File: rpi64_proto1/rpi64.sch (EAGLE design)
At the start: 115 parts, among them Q1 BSS123, Q2 BSS123

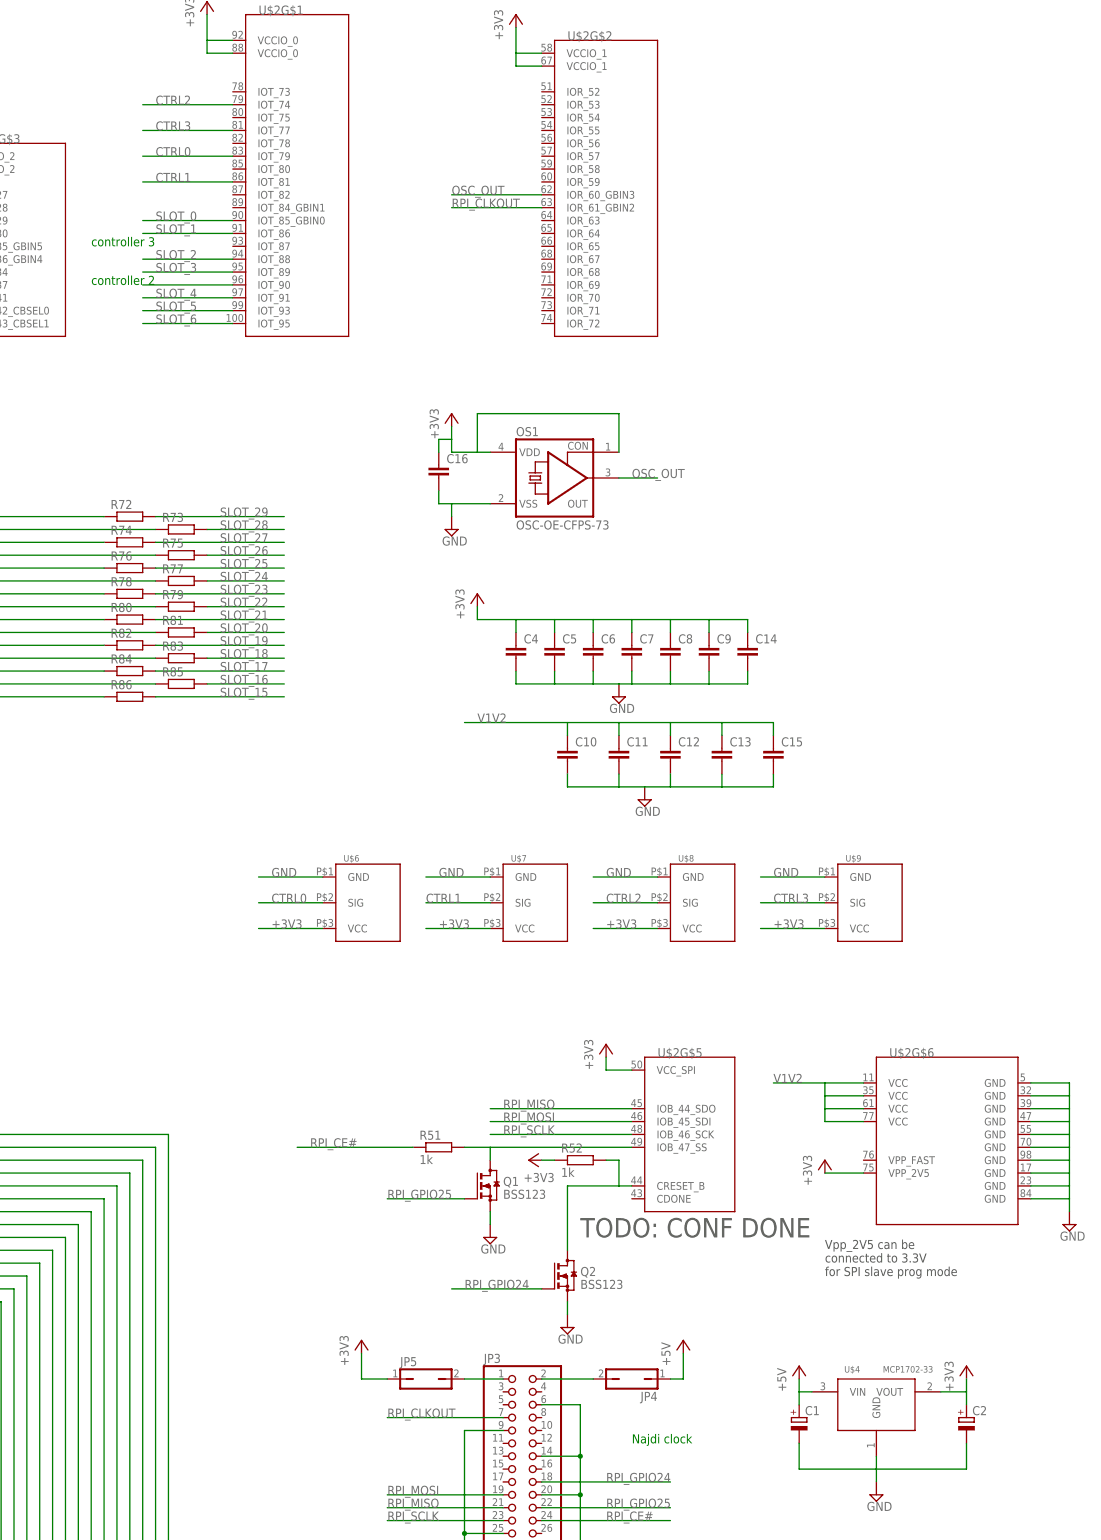
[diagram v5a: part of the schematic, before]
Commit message: Everything placed and routed
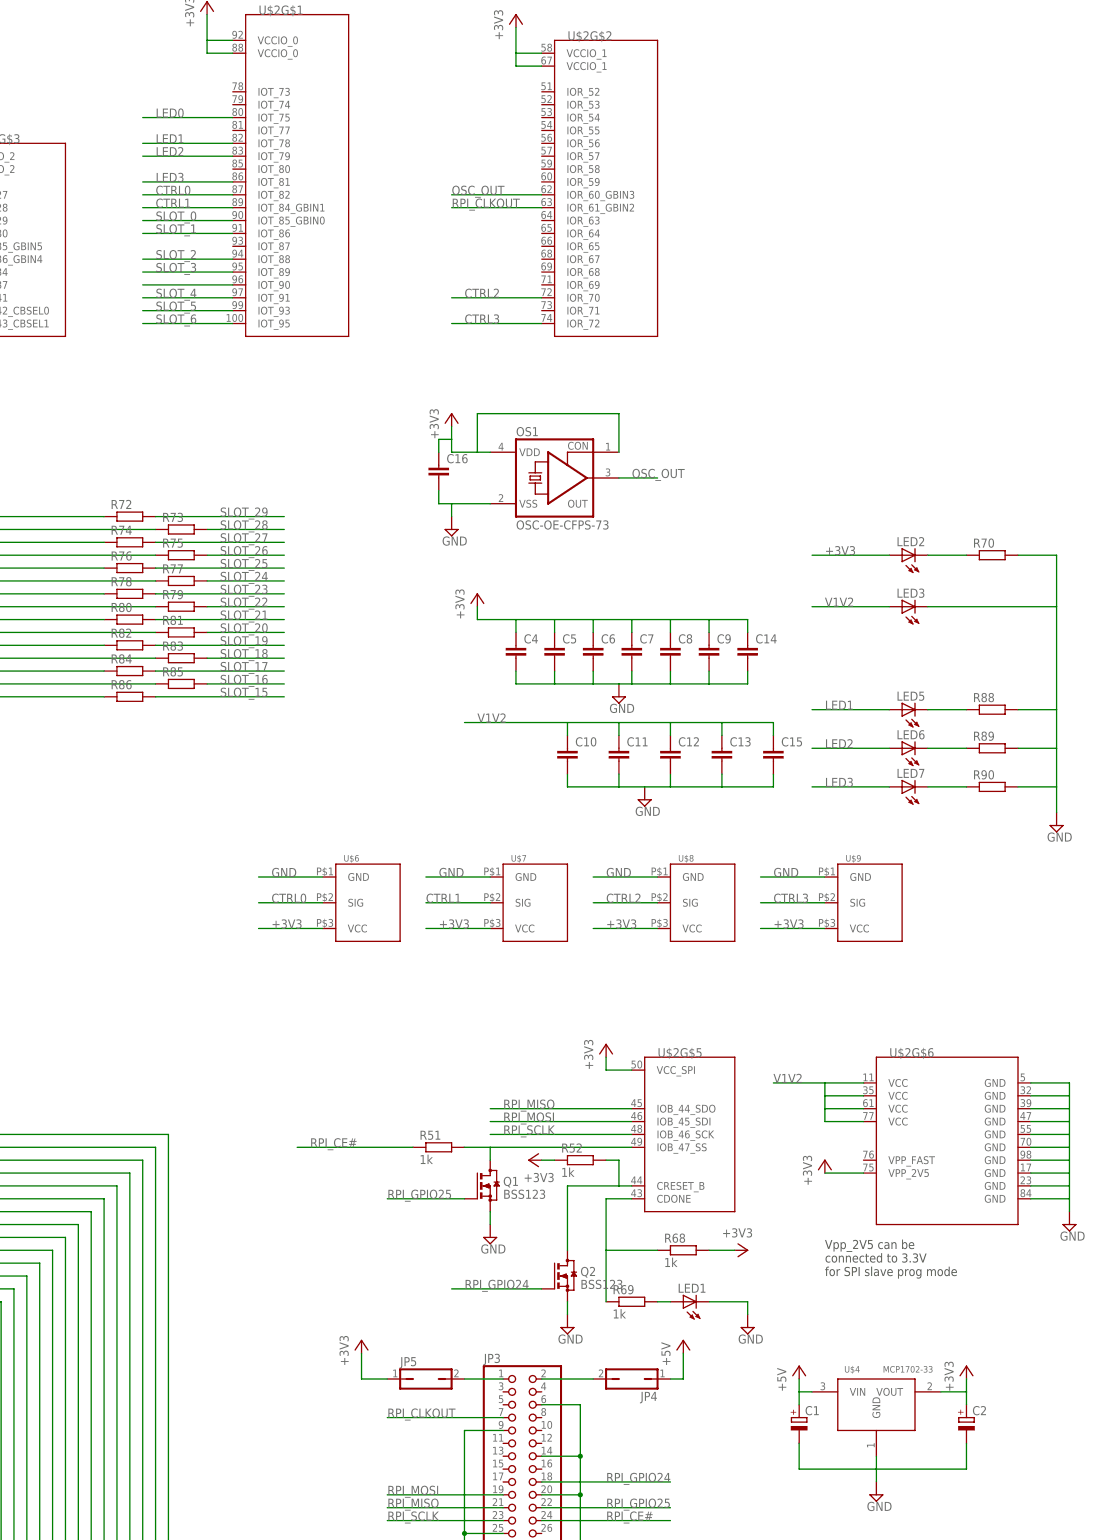
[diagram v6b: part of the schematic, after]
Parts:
- added LED1, LED2, LED3, LED5, LED6, LED7: (no value), led:LEDCHIPLED_0603
- added R68, R69: 1k, rcl:R-EU_R0603
- added R70, R88, R89, R90: (no value), rcl:R-EU_R0603
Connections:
- new net LED0: U$2G$1.IOT_75
- new net LED1: LED5.A, U$2G$1.IOT_78
- new net LED2: LED6.A, U$2G$1.IOT_79
- new net LED3: LED7.A, U$2G$1.IOT_81
- new net N$104: LED1.A, R69.2
- new net N$107: LED7.C, R90.1
- new net N$109: LED6.C, R89.1
- new net N$111: LED5.C, R88.1
- new net N$116: LED2.C, R70.1
- new net N$91: R68.1, R69.1, U$2G$5.CDONE
- net +3V3: now also LED2.A, R68.2
- net CTRL0: now also U$2G$1.IOT_82; no longer U$2G$1.IOT_79
- net CTRL1: now also U$2G$1.IOT_84_GBIN1; no longer U$2G$1.IOT_81
- net CTRL2: now also U$2G$2.IOR_70; no longer U$2G$1.IOT_74
- net CTRL3: now also U$2G$2.IOR_72; no longer U$2G$1.IOT_77
- net GND: now also LED1.C, LED3.C, R70.2, R88.2, R89.2, R90.2
- net V1V2: now also LED3.A
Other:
- note removed: "Najdi clock"
- note removed: "TODO: CONF DONE"
- note removed: "controller 2"
- note removed: "controller 3"

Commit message: Resolved DRC problems
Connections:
- removed net N$110: U$2G$1.IOT_90
- removed net N$113: U$2G$4.IOL_7A_GBIN6
- removed net N$114: U$2G$4.IOL_6B_GBIN7
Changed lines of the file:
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@@
 <pinref part="U$2" gate="G$6" pin="GND@9"/>
 <wire x1="388.62" y1="83.82" x2="396.24" y2="83.82" width="0.1524" layer="91"/>
+<junction x="396.24" y="104.14"/>
+<junction x="396.24" y="101.6"/>
+<junction x="396.24" y="99.06"/>
+<junction x="396.24" y="96.52"/>
+<junction x="396.24" y="93.98"/>
+<junction x="396.24" y="91.44"/>
+<junction x="396.24" y="88.9"/>
+<junction x="396.24" y="86.36"/>
+<junction x="396.24" y="83.82"/>
 </segment>
 <segment>
@@
 <wire x1="337.82" y1="167.64" x2="337.82" y2="165.1" width="0.1524" layer="91"/>
 <wire x1="337.82" y1="165.1" x2="327.66" y2="165.1" width="0.1524" layer="91"/>
+<junction x="307.34" y="165.1"/>
+<junction x="317.5" y="165.1"/>
+<junction x="327.66" y="165.1"/>
 </segment>
 <segment>
@@
 <wire x1="332.74" y1="187.96" x2="332.74" y2="185.42" width="0.1524" layer="91"/>
 <wire x1="332.74" y1="185.42" x2="325.12" y2="185.42" width="0.1524" layer="91"/>
+<junction x="325.12" y="185.42"/>
+<junction x="317.5" y="185.42"/>
+<junction x="309.88" y="185.42"/>
+<junction x="302.26" y="185.42"/>
+<junction x="294.64" y="185.42"/>
 </segment>
 <segment>
@@
 <pinref part="C2" gate="G$1" pin="+"/>
 <wire x1="375.92" y1="43.18" x2="375.92" y2="45.72" width="0.1524" layer="91"/>
+<junction x="375.92" y="45.72"/>
 </segment>
 <segment>
@@
 <wire x1="292.1" y1="307.34" x2="287.02" y2="307.34" width="0.1524" layer="91"/>
 <wire x1="287.02" y1="307.34" x2="287.02" y2="309.88" width="0.1524" layer="91"/>
+<junction x="287.02" y="309.88"/>
 </segment>
 <segment>
@@
 <wire x1="332.74" y1="195.58" x2="332.74" y2="198.12" width="0.1524" layer="91"/>
 <wire x1="332.74" y1="198.12" x2="325.12" y2="198.12" width="0.1524" layer="91"/>
+<junction x="287.02" y="198.12"/>
+<junction x="294.64" y="198.12"/>
+<junction x="302.26" y="198.12"/>
+<junction x="309.88" y="198.12"/>
+<junction x="317.5" y="198.12"/>
+<junction x="325.12" y="198.12"/>
 </segment>
 <segment>
@@
 <wire x1="307.34" y1="238.76" x2="279.4" y2="238.76" width="0.1524" layer="91"/>
 <wire x1="279.4" y1="238.76" x2="279.4" y2="231.14" width="0.1524" layer="91"/>
+<junction x="274.32" y="233.68"/>
 </segment>
 <segment>
@@
 <pinref part="C1" gate="G$1" pin="+"/>
 <wire x1="342.9" y1="43.18" x2="342.9" y2="45.72" width="0.1524" layer="91"/>
+<junction x="342.9" y="45.72"/>
 </segment>
 </net>
@@
 <wire x1="347.98" y1="106.68" x2="337.82" y2="106.68" width="0.1524" layer="91"/>
 <label x="337.82" y="106.68" size="1.778" layer="95"/>
+<junction x="347.98" y="104.14"/>
+<junction x="347.98" y="106.68"/>
+<junction x="347.98" y="101.6"/>
 </segment>
 <segment>
@@
 <wire x1="337.82" y1="175.26" x2="337.82" y2="177.8" width="0.1524" layer="91"/>
 <wire x1="337.82" y1="177.8" x2="327.66" y2="177.8" width="0.1524" layer="91"/>
+<junction x="327.66" y="177.8"/>
+<junction x="317.5" y="177.8"/>
+<junction x="307.34" y="177.8"/>
+<junction x="297.18" y="177.8"/>
 </segment>
 <segment>
@@
 <wire x1="281.94" y1="93.98" x2="276.86" y2="93.98" width="0.1524" layer="91"/>
 <wire x1="281.94" y1="91.44" x2="281.94" y2="93.98" width="0.1524" layer="91"/>
+<junction x="281.94" y="93.98"/>
 </segment>
 </net>
@@
 <wire x1="304.8" y1="91.44" x2="307.34" y2="91.44" width="0.1524" layer="91"/>
 <wire x1="307.34" y1="91.44" x2="307.34" y2="86.36" width="0.1524" layer="91"/>
+<junction x="307.34" y="86.36"/>
 </segment>
 </net>
@@
 </segment>
 </net>
-<net name="N$110" class="0">
-<segment>
-<pinref part="U$2" gate="G$1" pin="IOT_90"/>
-<wire x1="231.14" y1="264.16" x2="213.36" y2="264.16" width="0.1524" layer="91"/>
-</segment>
-</net>
-<net name="N$113" class="0">
-<segment>
-<pinref part="U$2" gate="G$4" pin="IOL_7A_GBIN6"/>
-<wire x1="111.76" y1="276.86" x2="88.9" y2="276.86" width="0.1524" layer="91"/>
-</segment>
-</net>
-<net name="N$114" class="0">
-<segment>
-<pinref part="U$2" gate="G$4" pin="IOL_6B_GBIN7"/>
-<wire x1="111.76" y1="279.4" x2="88.9" y2="279.4" width="0.1524" layer="91"/>
-</segment>
-</net>
 <net name="SLOT_15" class="0">
 <segment>
@@
 <wire x1="304.8" y1="73.66" x2="304.8" y2="83.82" width="0.1524" layer="91"/>
 <wire x1="314.96" y1="73.66" x2="304.8" y2="73.66" width="0.1524" layer="91"/>
+<junction x="304.8" y="73.66"/>
 </segment>
 </net>
@@
 </sheet>
 </sheets>
+<errors>
+</errors>
 </schematic>
 </drawing>
